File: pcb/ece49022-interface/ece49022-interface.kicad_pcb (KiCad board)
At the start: 4 copper layers, 60.2 x 52.2 mm, 40 parts, among them J1 Conn_01x04_Pin, J10 Conn_01x06_Pin, J2 Conn_01x05_Pin, J3 Conn_01x04_Pin, J4 Conn_01x04_Pin, J5 Conn_01x04_Pin, J6 Conn_01x02_Pin, J7 Conn_01x04_Pin, J8 Conn_01x04_Pin, Q1 KSC1815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

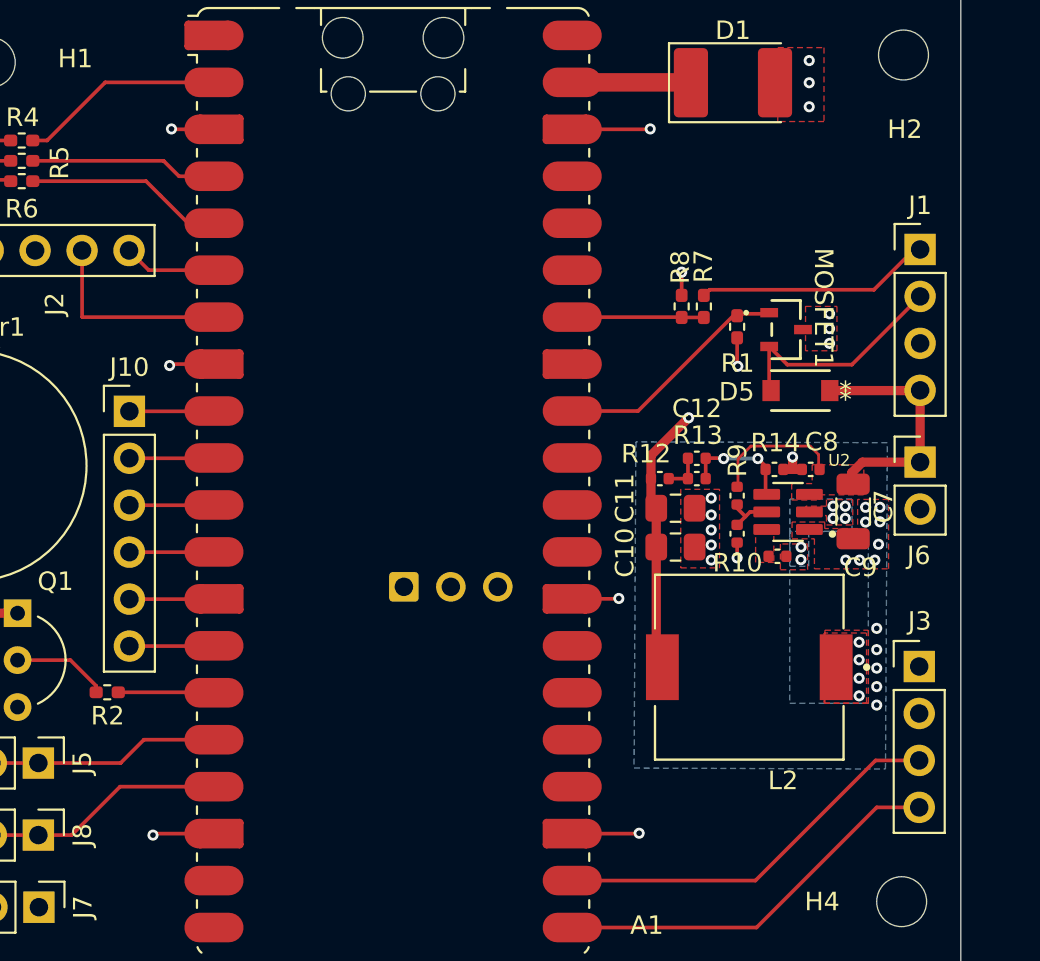
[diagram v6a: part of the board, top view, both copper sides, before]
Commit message: fixed some stuff in interface and changed trace width for 50 ohm in shelf pcb
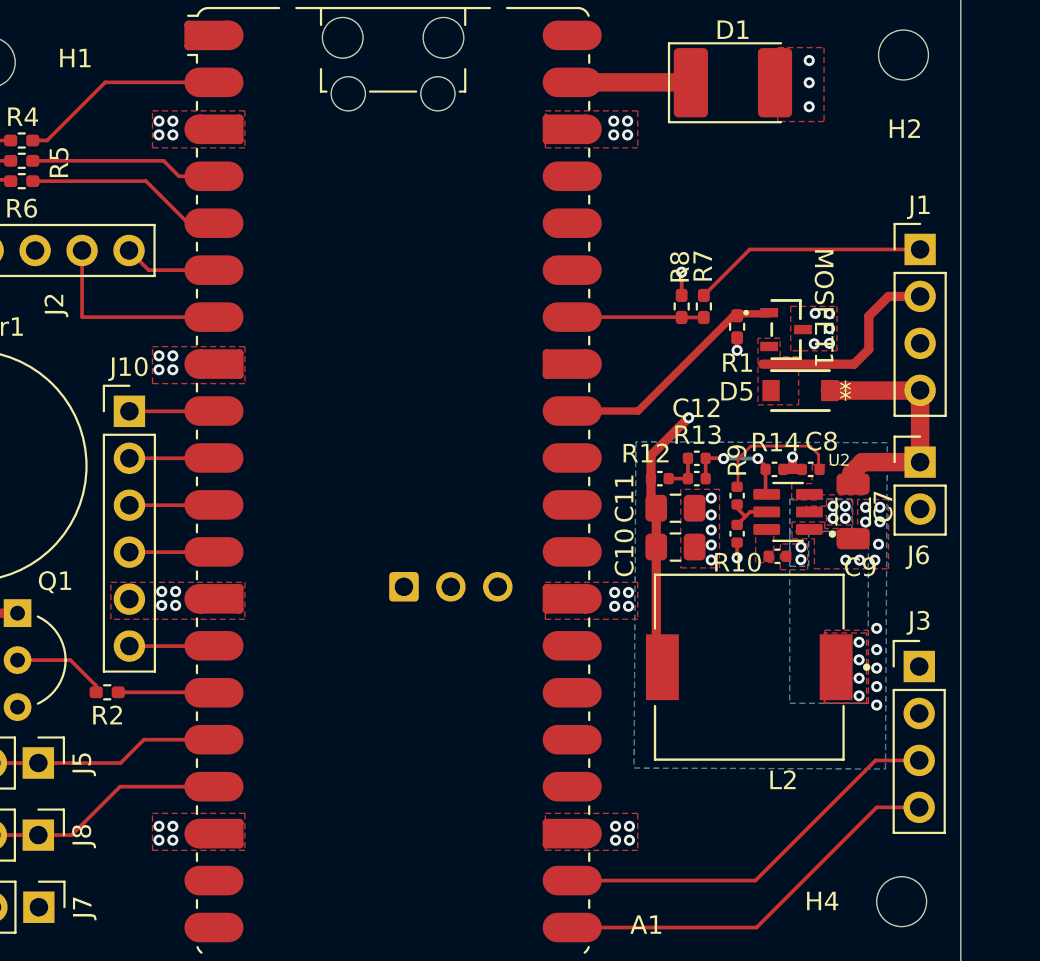
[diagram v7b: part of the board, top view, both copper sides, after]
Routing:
- net GND: track 28.9 -> 4.67 mm, vias 31 -> 55
- net /LOCK_RTN: track 12.5 -> 11.1 mm
- added copper zone on F.Cu, net /LOCK_RTN
